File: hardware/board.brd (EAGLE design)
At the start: 100 x 100 mm, 84 parts, among them CON1 USB-FPGA1.11, CON2 USB-FPGA-2THT, IC1 THS3062

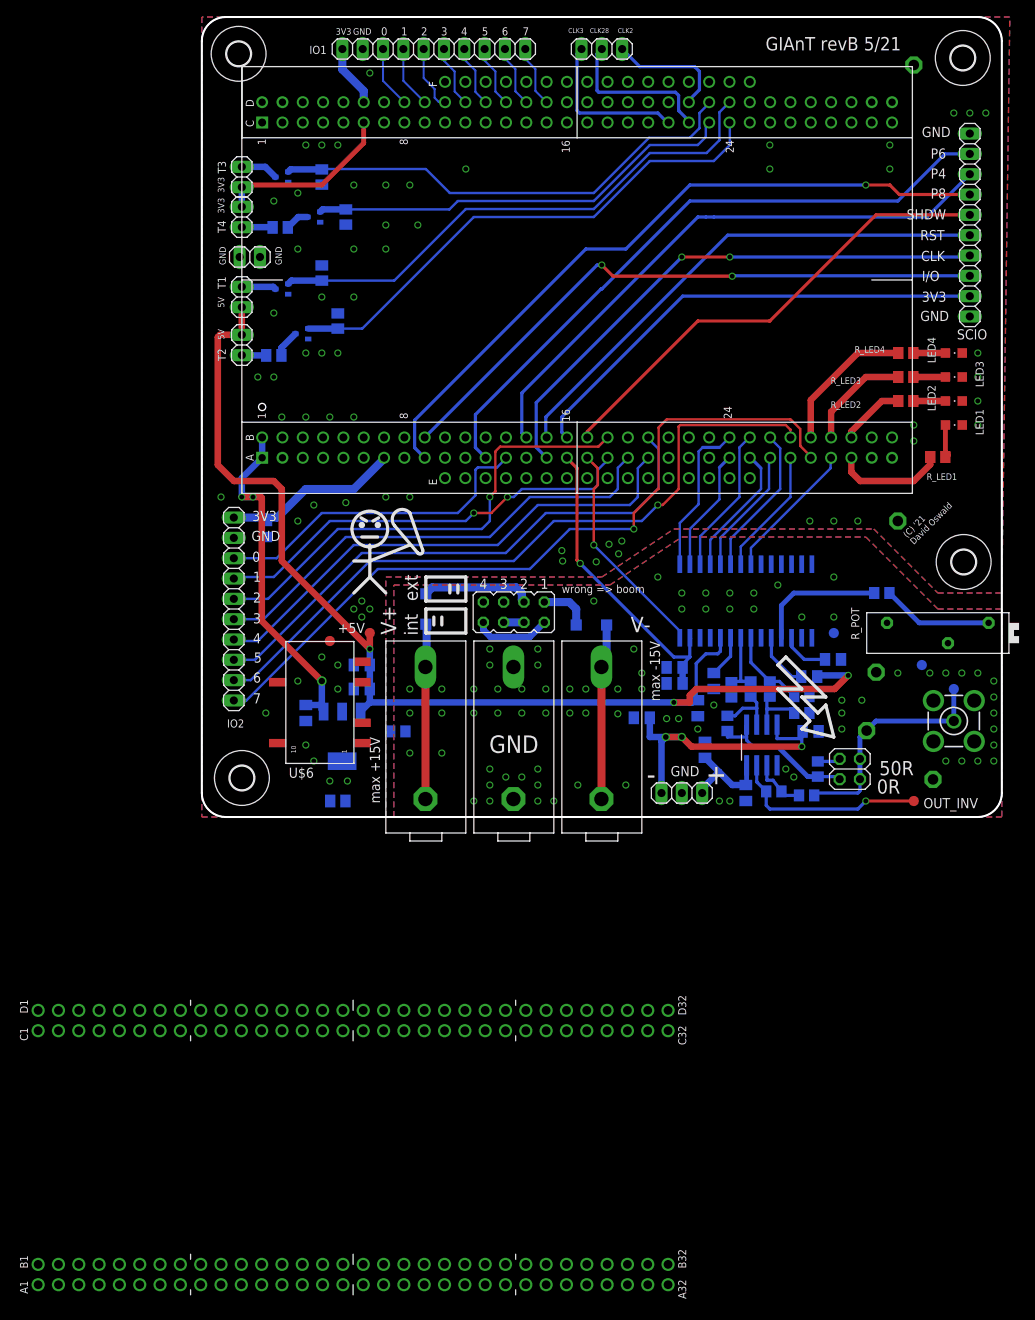
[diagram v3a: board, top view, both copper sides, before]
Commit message: Fully routed (no ADC)
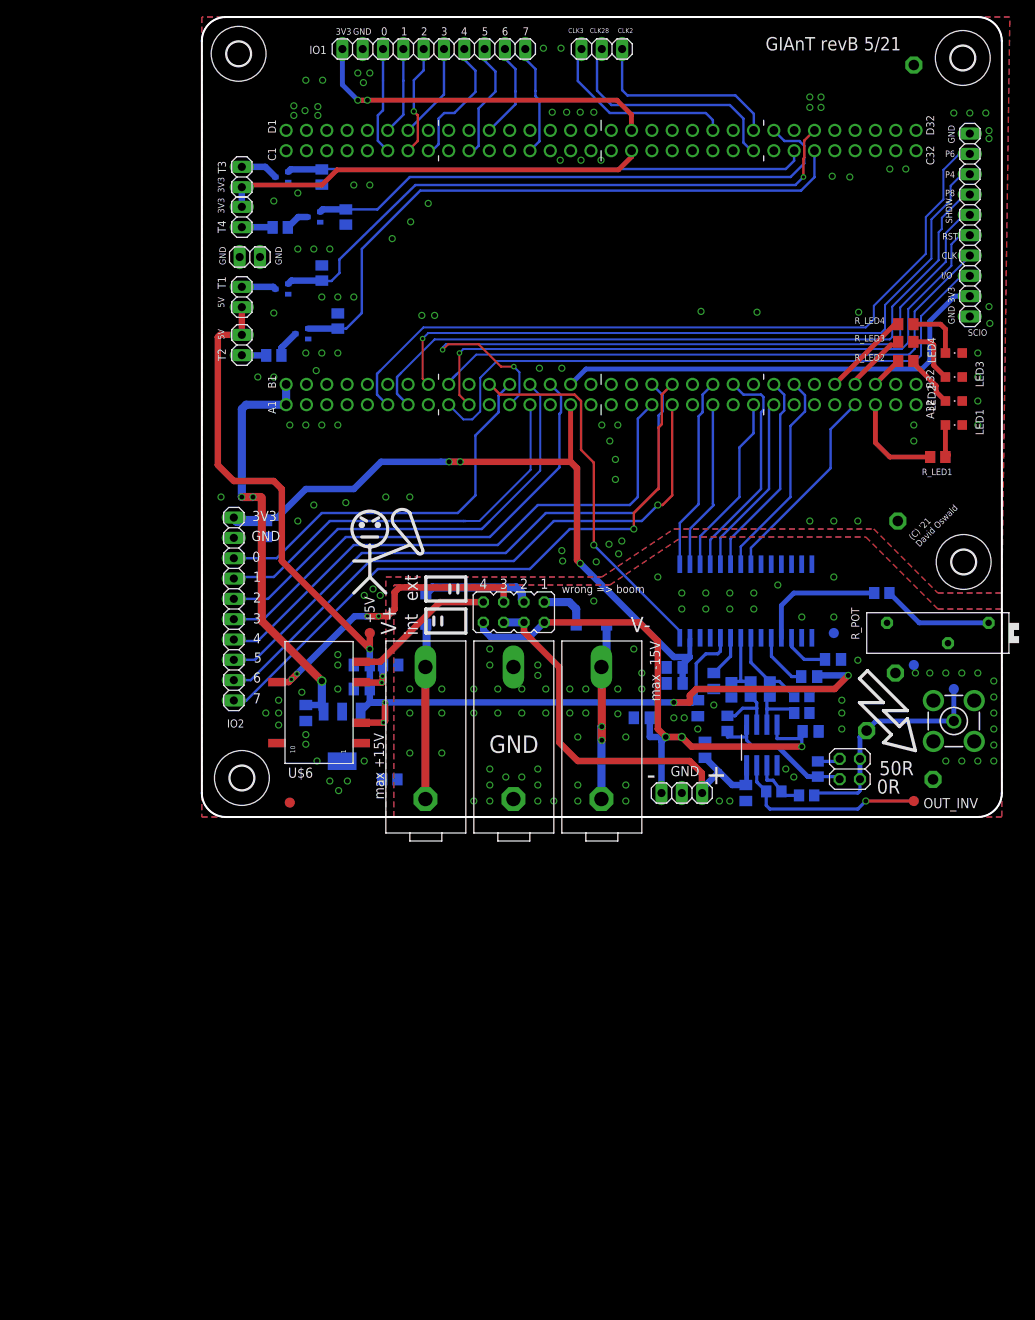
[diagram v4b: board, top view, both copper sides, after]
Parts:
- removed CON1: USB-FPGA1.11, usb-fpga-1:USB-FPGA1.11
- moved CON2 114.3 mm to (8.00, 49.0)
- moved TP_GND 20.8 mm to (11.0, 1.80)
- moved R7 18.2 mm to (23.6, 19.0)
- moved R_GND1 6.08 mm to (23.5, 4.70)
- moved R_LED2 5.00 mm to (88.0, 57.0)
- moved R_LED3 4.40 mm to (88.0, 59.4)
- moved R_LED4 3.60 mm to (88.0, 61.6)
- moved TP3 2.40 mm to (86.7, 18.0)
- moved TP_GND1 1.00 mm to (89.0, 19.0)
- moved U$6 0.10 mm to (10.4, 6.70)
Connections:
- removed net N$69: CON1.C20
- removed net VCCIO: C19.1, CON1.A7, GPIO2.1
- net +5V/1: now also C19.1, GPIO2.1; no longer CON1.A16
- net +5V/2: no longer CON1.D6
- net +5V/3: no longer CON1.C6
- net CLK_SC: no longer CON1.A15
- net DAC_CLK: no longer CON1.A17
- net DB0: no longer CON1.A29
- net DB1: no longer CON1.A27
- net DB2: no longer CON1.B26
- net DB3: no longer CON1.A26
- net DB4: no longer CON1.A25
- net DB5: no longer CON1.B25
- net DB6: no longer CON1.A24
- net DB7: no longer CON1.B24
- net GCLK2: no longer CON1.D22
- net GCLK28: no longer CON1.C22
- net GCLK3: no longer CON1.C21
- net GND: no longer CON1.A2, CON1.A21, CON1.A32, CON1.B13, CON1.B2, CON1.B21, CON1.B32, CON1.B5, CON1.C17, CON1.C26, CON1.C32, CON1.C4, CON1.C8, CON1.D26, CON1.D4
- net GPIO0: no longer CON1.D8
- net GPIO1: no longer CON1.D9
- net GPIO2: no longer CON1.D10
- net GPIO2_0: no longer CON1.A13
- net GPIO2_1: no longer CON1.A18
- net GPIO2_2: no longer CON1.B18
- net GPIO2_3: no longer CON1.A19
- net GPIO2_4: no longer CON1.A20
- net GPIO2_5: no longer CON1.B20
- net GPIO2_6: no longer CON1.B27
- net GPIO2_7: no longer CON1.A28
- net GPIO3: no longer CON1.D11
- net GPIO4: no longer CON1.D12
- net GPIO5: no longer CON1.D13
- net GPIO6: no longer CON1.D14
- net GPIO7: no longer CON1.D15
- net IO: no longer CON1.B9
- net LED1_PIN: no longer CON1.A30
- net LED2_PIN: no longer CON1.B30
- net LED3_PIN: no longer CON1.B29
- net LED4_PIN: no longer CON1.B28
- net PIN4: no longer CON1.B14
- net PIN6: no longer CON1.A12
- net PIN8: no longer CON1.A9
- net RST: no longer CON1.B15
- net SHDN: no longer CON1.B17
- net SW1: no longer CON1.B12
- net SW2: no longer CON1.A14
- net T1: no longer CON1.D24
- net T2: no longer CON1.C24
- net T3: no longer CON1.D23
- net T4: no longer CON1.C23
- net VEE: no longer CON1.A1, CON1.B1
- net VPP: no longer CON1.B16
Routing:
- net +5V/1: track 38.6 -> 92.0 mm, vias 1 -> 3
- net VCC+: track 15.1 -> 53.8 mm
- net +9V: track 0.00 -> 38.7 mm, vias 0 -> 4
- net +5V/2: track 7.75 -> 45.3 mm, vias 0 -> 2
- net SHDN: track 59.8 -> 93.2 mm, vias 0 -> 2
- net +5V/3: track 22.6 -> 53.5 mm
- net VCC-: track 47.7 -> 75.2 mm
- net VCCIO: track 22.3 -> 0.00 mm
- net DAC_CLK: track 27.7 -> 47.0 mm
- net -9V: track 0.00 -> 18.4 mm
- net GPIO2_7: track 95.7 -> 79.0 mm
- net RST: track 65.0 -> 80.9 mm, vias 0 -> 1
- net T4: track 54.1 -> 69.8 mm
- net PIN4: track 73.1 -> 88.6 mm, vias 0 -> 1
- net PIN6: track 81.2 -> 95.8 mm
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
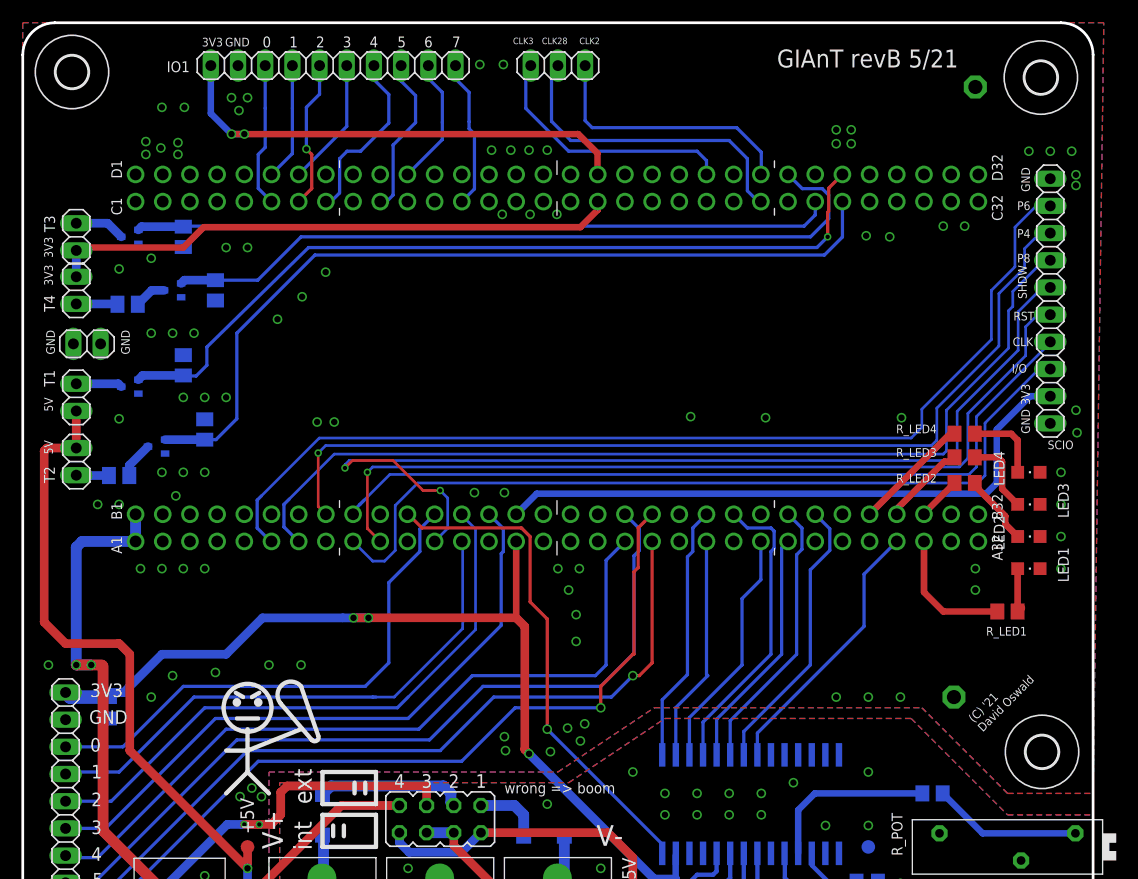
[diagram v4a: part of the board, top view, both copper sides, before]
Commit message: Fully routed and freed some space for ADC in middle/right
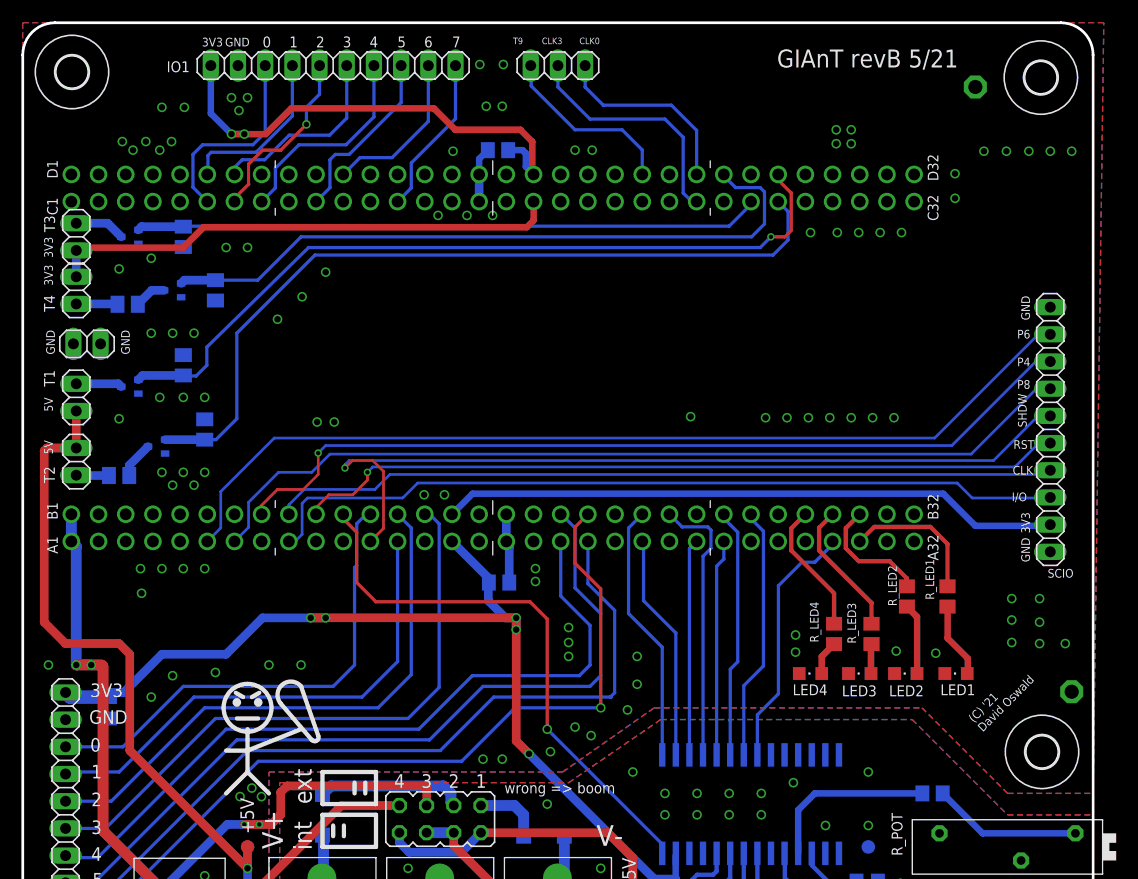
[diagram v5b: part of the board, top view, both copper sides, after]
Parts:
- added R10, R8: 0, rcl:R0805
- moved LED4 27.7 mm to (73.6, 39.2), turned to 90 degrees
- moved LED3 22.3 mm to (78.2, 39.2), turned to 90 degrees
- moved R_LED4 22.3 mm to (75.8, 42.9), turned to 90 degrees
- moved R_LED3 18.7 mm to (79.3, 42.9), turned to 90 degrees
- moved LED2 17.2 mm to (82.5, 39.2), turned to 90 degrees
- moved SCIO 12.0 mm to (96.0, 62.0)
- moved LED1 11.9 mm to (87.2, 39.2), turned to 90 degrees
- moved R_LED2 11.9 mm to (82.6, 46.4), turned to 90 degrees
- moved TP_GNDA 11.0 mm to (98.0, 37.5)
- moved CON2 6.00 mm to (2.00, 49.0)
- moved R_LED1 5.77 mm to (86.4, 46.4), turned to 90 degrees
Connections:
- net GCLK2 renamed GCLK0
- removed net GCLK28: CON2.C24, JP7.2
- new net FPGA_T9: CON2.D22, JP7.1
- new net N$1: CON2.A17, CON2.B17, R10.2
- new net N$2: CON2.C16, CON2.D16, R8.2
- net +5V/1: now also R10.1
- net +5V/2: now also R8.1
- net GCLK3: now also CON2.C24, JP7.2; no longer CON2.D22, JP7.1
- net RST: now also CON2.B10; no longer CON2.A10
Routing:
- net GCLK28: track 29.9 -> 0.00 mm
- net FPGA_T9: track 0.00 -> 17.1 mm
- net SHDN: track 93.2 -> 79.5 mm, vias 2 -> 1
- net RST: track 80.9 -> 72.1 mm
- net PIN4: track 88.6 -> 81.3 mm
- net LED2_PIN: track 4.17 -> 11.3 mm
- net N$1: track 0.00 -> 7.14 mm
- net PIN6: track 95.8 -> 88.8 mm
- net GCLK0: track 24.9 -> 18.2 mm
- net PIN8: track 90.2 -> 83.5 mm
- net T3: track 65.1 -> 58.5 mm
- net LED3_PIN: track 7.24 -> 12.8 mm
- net T4: track 69.8 -> 64.4 mm
- net DAC_CLK: track 47.0 -> 52.5 mm
- net +5V/3: track 53.5 -> 48.1 mm
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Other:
- board text added: "CLK0"
- board text added: "T9"
- board text removed: "CLK2"
- board text removed: "CLK28"

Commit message: Added ADC schematics etc, missing: FPGA pins and routing
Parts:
- added C11, C12: 1µ, rcl:C1206
- added C13: 100n, rcl:C0805
- added CD1, CD3, CD6, CD8, CD_AMP, C_DEC_IN, C_DEC_OUT, C_REF1, C_REF3, C_REF4, C_REF6: 100n, rcl:C0603
- added CD2, CD4, CD5: 10n, rcl:C0603
- added CD9: 4.7µ, rcl:C1206
- added C_F+, C_F-: opt., rcl:C0603
- added C_REF2, C_REF5: 10µ, rcl:C1206
- added IC2: AD80XX, ad80xx:SO08
- added L1: 120n, footprint?, SparkFun:0805
- added R11, R12: 10k, rcl:R0805
- added R9: optional, rcl:R0805
- added R_F+, R_F-, R_T_IN: 49, rcl:R0603
- added R_FB+, R_FB-: 1k, rcl:R0603
- added R_FI, R_GI: 20k, rcl:R0603
- added R_GND: 0, rcl:R0805
- added R_IN+: 499, rcl:R0603
- added R_IN-: 523, rcl:R0603
- added SJ1, SJ2: 0R, jumper:SJ
- added TP_GNDA1, TP_IN: TPPAD1-13, testpad:P1-13
- added U$18: TS5204, ts5204:SOT23
- added U$7: AD8138, ad8138:SOIC8
- added U1: AD9215BRUZ, ad9215bruz:TSSOP28
- added X1: BU-SMA-V, con-coax-sma-adapted:BU-SMA-V
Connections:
- new net ADC_CLK: R9.2, SJ2.1, U1.13
- new net ADC_CLK_FB: SJ2.2
- new net ADC_D0: U1.17
- new net ADC_D1: U1.18
- new net ADC_D2: U1.19
- new net ADC_D3: U1.20
- new net ADC_D4: U1.21
- new net ADC_D5: U1.22
- new net ADC_D6: U1.25
- new net ADC_D7: U1.26
- new net ADC_D8: U1.27
- new net ADC_D9: U1.28
- new net ADC_IN+: C_F+.2, R_F+.1, U1.9
- new net ADC_IN-: C_F-.1, R_F-.1, U1.10
- new net ADC_OR: U1.1
- new net ADC_V_REF: C_REF5.2, C_REF6.2, SJ1.1, U1.4
- new net AMP_IN+: R_FB-.2, R_IN+.1, U$7.8
- new net AMP_IN-: R_FB+.1, R_IN-.1, U$7.1
- new net AMP_OUT+: R_F+.2, R_FB+.2, U$7.4
- new net AMP_OUT-: R_F-.2, R_FB-.1, U$7.5
- new net GND2: C11.2, C12.2, C13.2, CD1.2, CD2.2, CD3.2, CD4.2, CD8.2, CD9.1, CD_AMP.2, C_F+.1, C_F-.2, C_REF3.1, C_REF4.1, C_REF5.1, C_REF6.1, R12.1, R_GND.1, R_IN-.2, R_T_IN.2, TP_GNDA1.TP, U$18.3, U$7.6, U1.11, U1.14, U1.2, U1.8, X1.2, X1.3, X1.4, X1.5
- new net IN_ADC_AMP: C_DEC_OUT.2, R_IN+.2, R_T_IN.1
- new net N$21: C_DEC_OUT.1, IC2.1, R_FI.2
- new net N$25: IC2.2, R_FI.1, R_GI.2
- new net N$3: C11.1, L1.1, U$18.2
- new net N$4: SJ1.2, U1.3
- new net N$5: C_REF1.2, C_REF2.2, C_REF3.2, U1.6
- new net N$6: C_REF1.1, C_REF2.1, C_REF4.2, U1.5
- new net N$8: C_DEC_IN.1, TP_IN.TP, X1.1
- new net N$9: C_DEC_IN.2, IC2.3
- new net OP-: IC2.4
- new net VCC_ADC: CD5.1, CD6.1, U1.24
- new net V_15: IC2.6, IC2.7, R_GI.1, U$7.2
- new net V_15_UNBUF: C13.1, IC2.5, R11.1, R12.2
- new net V_ANALOG: C12.1, CD1.1, CD2.1, CD3.1, CD4.1, CD8.1, CD9.2, CD_AMP.1, IC2.8, R11.2, U$18.1, U$7.3, U1.12, U1.7
- net +5V/3: now also L1.2
- net GND: now also CD5.2, CD6.2, R9.1, R_GND.2, U1.23

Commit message: Added ADC pins (unrouted) Moved GCLK pins
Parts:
- moved SJ2 173.5 mm to (59.0, 76.0), flipped to the bottom, turned to 180 degrees
- moved L1 151.2 mm to (30.0, 75.0), flipped to the bottom, turned to 270 degrees
- moved U$18 135.9 mm to (30.0, 71.0), flipped to the bottom
- moved U1 7.07 mm to (48.0, 70.0), turned to 90 degrees
- moved U$7 5.39 mm to (68.0, 71.0)
- moved IC2 4.24 mm to (80.0, 71.0)
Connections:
- removed net FPGA_T9: CON2.D22, JP7.1
- removed net GCLK0: CON2.D24, JP7.3
- removed net GCLK3: CON2.C24, JP7.2
- new net DAC_SLEEP: AD9708.15
- new net FPGA_R9: CON2.D23, JP7.1
- new net GCLK2: CON2.C25, JP7.2
- new net GCLK28: CON2.D26, JP7.3
- net ADC_CLK: now also CON2.D24
- net ADC_CLK_FB: now also CON2.C24
- net ADC_D0: now also CON2.C15
- net ADC_D1: now also CON2.D15
- net ADC_D2: now also CON2.C19
- net ADC_D3: now also CON2.D19
- net ADC_D4: now also CON2.C20
- net ADC_D5: now also CON2.D20
- net ADC_D6: now also CON2.C21
- net ADC_D7: now also CON2.D21
- net ADC_D8: now also CON2.C22
- net ADC_D9: now also CON2.D22
- net ADC_OR: now also CON2.C23
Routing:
- net GCLK2: track 0.00 -> 23.5 mm
- net GCLK3: track 22.4 -> 0.00 mm
- net GCLK28: track 0.00 -> 20.9 mm
- net FPGA_R9: track 0.00 -> 18.3 mm
- net GCLK0: track 18.2 -> 0.00 mm
- net FPGA_T9: track 17.1 -> 0.00 mm
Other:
- board text added: "CLK2"
- board text added: "CLK28"
- board text added: "R9"
- board text removed: "CLK0"
- board text removed: "CLK3"
- board text removed: "T9"

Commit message: Placed ADC components Changed ADC VR
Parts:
- removed CD8, CD_AMP, C_DEC_IN, C_DEC_OUT, C_REF6: 100n, rcl:C0603
- removed CD9: 4.7µ, rcl:C1206
- removed C_F+, C_F-: opt., rcl:C0603
- removed C_REF2, C_REF5: 10µ, rcl:C1206
- removed R_F+, R_F-, R_T_IN: 49, rcl:R0603
- removed R_FB+, R_FB-: 1k, rcl:R0603
- removed R_FI, R_GI: 20k, rcl:R0603
- removed R_GND: 0, rcl:R0805
- removed R_IN+: 499, rcl:R0603
- removed R_IN-: 523, rcl:R0603
- added C15, C21, C22, CIN, CR6: 100n, rcl:C0603
- added C23: 4.7µ, rcl:C0805K
- added CF+, CF-: opt., rcl:C0603
- added CR2, CR5: 10µ, rcl:C0805K
- added R+: 499, rcl:R0603
- added R-: 523, rcl:R0603
- added R20: 0, rcl:R0805
- added RF+, RF-, RT: 49, rcl:R0603
- added RFB+, RFB-: 1k, rcl:R0603
- added RFI, RGI: 20k, rcl:R0603
- added TP_IN1: TPPAD1-13, testpad:P1-13
- C11, C12: device rcl:C1206 -> rcl:C0805K
- U$18: value TS5204 -> XC6206P302MRN; device ts5204:SOT23 -> XC6206:SOT23
- moved TP_IN 259.8 mm to (94.2, 86.3)
- moved C13 230.3 mm to (89.2, 72.2), flipped to the bottom, turned to 90 degrees
- moved R12 229.0 mm to (84.0, 66.5), flipped to the bottom
- moved R11 217.5 mm to (78.5, 69.6), flipped to the bottom, turned to 90 degrees
- moved CD5 192.6 mm to (35.0, 73.0), flipped to the bottom, turned to 90 degrees
- moved SJ1 187.1 mm to (46.2, 64.5), flipped to the bottom, turned to 180 degrees
- moved CD6 185.5 mm to (32.6, 73.0), flipped to the bottom, turned to 90 degrees
- moved R9 169.7 mm to (54.5, 74.8), flipped to the bottom, turned to 90 degrees
- moved TP_GNDA1 144.4 mm to (72.3, 65.3)
- moved C11 137.0 mm to (25.0, 67.0), flipped to the bottom, turned to 180 degrees
- moved C12 136.1 mm to (33.6, 65.1), flipped to the bottom, turned to 180 degrees
- moved SJ2 8.96 mm to (50.2, 74.3), turned to 0 degrees
- moved U$7 6.81 mm to (61.3, 69.8), turned to 0 degrees
- moved U1 5.90 mm to (42.1, 70.0), turned to 0 degrees
- moved L1 5.48 mm to (26.6, 70.7), turned to 90 degrees
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- renumbered C_REF1 to CR1, C_REF3 to CR3, C_REF4 to CR4
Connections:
- removed net VCC_ADC: CD5.1, CD6.1, U1.24
- net +5V/3: now also CD5.1, CD6.1, U1.24
- net ADC_IN+: now also CF+.2, RF+.1; no longer C_F+.2, R_F+.1
- net ADC_IN-: now also CF-.1, RF-.1; no longer C_F-.1, R_F-.1
- net ADC_V_REF: now also CR5.2, CR6.2; no longer C_REF5.2, C_REF6.2
- net AMP_IN+: now also R+.1, RFB-.2; no longer R_FB-.2, R_IN+.1
- net AMP_IN-: now also R-.1, RFB+.1; no longer R_FB+.1, R_IN-.1
- net AMP_OUT+: now also RF+.2, RFB+.2; no longer R_F+.2, R_FB+.2
- net AMP_OUT-: now also RF-.2, RFB-.1; no longer R_F-.2, R_FB-.1
- net GND: now also R20.2; no longer R_GND.2
- net GND2: now also C21.2, C22.2, C23.1, CF+.1, CF-.2, CR5.1, CR6.1, R-.2, R20.1, RT.2, U$18.1; no longer CD8.2, CD9.1, CD_AMP.2, C_F+.1, C_F-.2, C_REF5.1, C_REF6.1, R_GND.1, R_IN-.2, R_T_IN.2, U$18.3
- net IN_ADC_AMP: now also C15.2, R+.2, RT.1, TP_IN1.TP; no longer C_DEC_OUT.2, R_IN+.2, R_T_IN.1
- net N$21: now also C15.1, RFI.2; no longer C_DEC_OUT.1, R_FI.2
- net N$25: now also RFI.1, RGI.2; no longer R_FI.1, R_GI.2
- net N$3: now also U$18.3; no longer U$18.2
- net N$5: now also CR2.2; no longer C_REF2.2
- net N$6: now also CR2.1; no longer C_REF2.1
- net N$8: now also CIN.1; no longer C_DEC_IN.1
- net N$9: now also CIN.2; no longer C_DEC_IN.2
- net V_15: now also RGI.1; no longer R_GI.1
- net V_ANALOG: now also C21.1, C22.1, C23.2, U$18.2; no longer CD8.1, CD9.2, CD_AMP.1, U$18.1
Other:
- board text added: "GIAnT revB 6/21"
- board text removed: "GIAnT revB 5/21"
